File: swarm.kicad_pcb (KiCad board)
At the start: 2 copper layers, 1 part, among them U1 STM32F103RETx

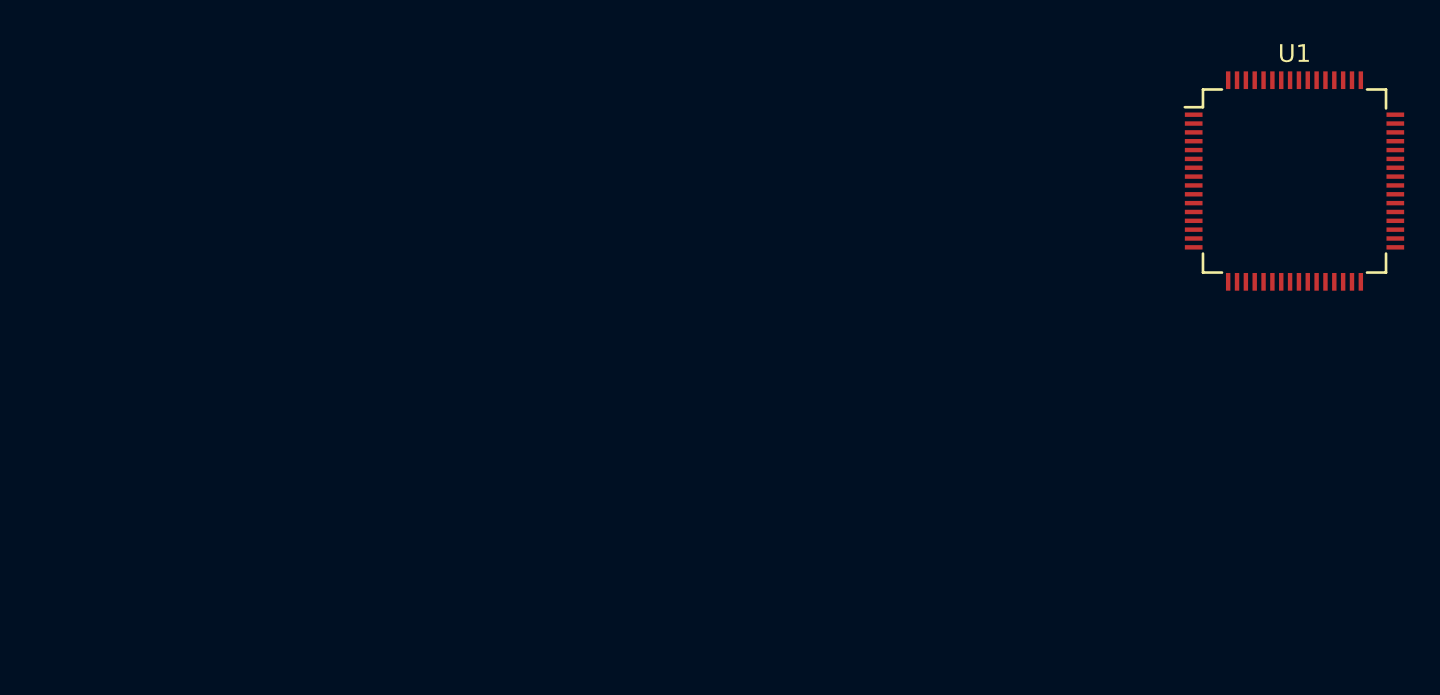
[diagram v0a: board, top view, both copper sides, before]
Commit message: Updates netlist, footprint selection
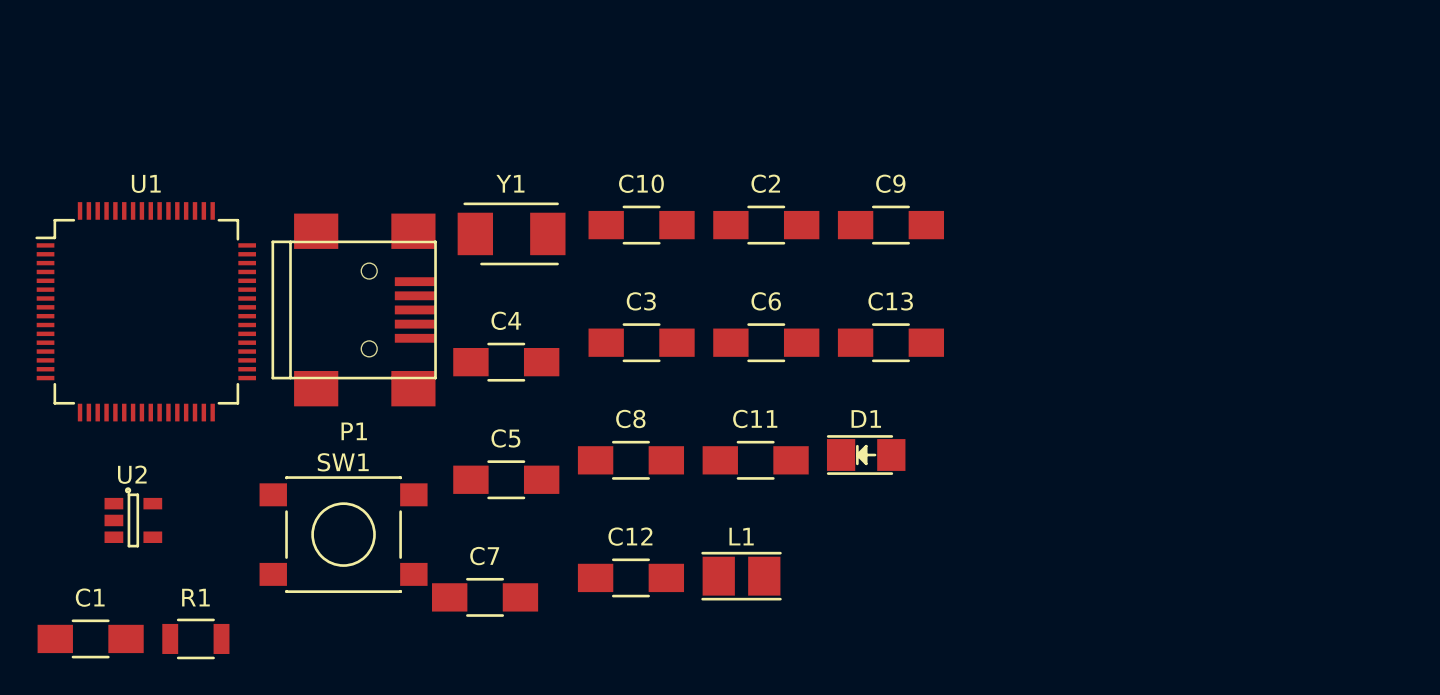
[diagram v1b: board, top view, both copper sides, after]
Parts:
- added C1: 10uF, Capacitors_SMD:C_1206_HandSoldering, F.Cu at (80.4, 130.9)
- added C10: 100n, Capacitors_SMD:C_1206_HandSoldering, F.Cu at (111.6, 107.5)
- added C11: 100n, Capacitors_SMD:C_1206_HandSoldering, F.Cu at (118.0, 120.8)
- added C12: 100n, Capacitors_SMD:C_1206_HandSoldering, F.Cu at (111.0, 127.4)
- added C13: 100n, Capacitors_SMD:C_1206_HandSoldering, F.Cu at (125.7, 114.1)
- added C2: 22uF, Capacitors_SMD:C_1206_HandSoldering, F.Cu at (118.6, 107.5)
- added C3: C, Capacitors_SMD:C_1206_HandSoldering, F.Cu at (111.6, 114.1)
- added C4: 100n, Capacitors_SMD:C_1206_HandSoldering, F.Cu at (103.9, 115.2)
- added C5: C, Capacitors_SMD:C_1206_HandSoldering, F.Cu at (103.9, 121.9)
- added C6: 1u, Capacitors_SMD:C_1206_HandSoldering, F.Cu at (118.6, 114.1)
- added C7: 10u, Capacitors_SMD:C_1206_HandSoldering, F.Cu at (102.7, 128.5)
- added C8: 100n, Capacitors_SMD:C_1206_HandSoldering, F.Cu at (111.0, 120.8)
- added C9: 100n, Capacitors_SMD:C_1206_HandSoldering, F.Cu at (125.7, 107.5)
- added D1: LED, LEDs:LED_1206, F.Cu at (124.3, 120.5)
- added L1: 2.2uH, Inductors:Inductor_Taiyo-Yuden_NR-24xx_HandSoldering, F.Cu at (117.2, 127.3)
- added P1: USB_OTG, Connect:USB_Mini-B, F.Cu at (95.3, 112.3)
- added R1: 330, Resistors_SMD:R_1206, F.Cu at (86.4, 130.9)
- added SW1: SW_PUSH, Buttons_Switches_SMD:SW_SPST_PTS645, F.Cu at (94.7, 125.0)
- added U2: LM3671MF-3.3, TO_SOT_Packages_SMD:SOT-23-5, F.Cu at (82.9, 124.2)
- added Y1: Crystal, Crystals:Crystal_SMD_5032_2Pads, F.Cu at (104.2, 108.0)
- moved U1 65.3 mm to (83.6, 112.4)
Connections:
- U1 pad 1: (no net) -> +3V3
- U1 pad 10: (no net) -> Net-(U1-Pad10)
- U1 pad 11: (no net) -> Net-(U1-Pad11)
- U1 pad 14: (no net) -> Net-(U1-Pad14)
- U1 pad 15: (no net) -> Net-(U1-Pad15)
- U1 pad 16: (no net) -> Net-(U1-Pad16)
- U1 pad 17: (no net) -> Net-(U1-Pad17)
- U1 pad 2: (no net) -> Net-(U1-Pad2)
- U1 pad 20: (no net) -> Net-(U1-Pad20)
- U1 pad 21: (no net) -> Net-(U1-Pad21)
- U1 pad 22: (no net) -> Net-(U1-Pad22)
- U1 pad 23: (no net) -> Net-(U1-Pad23)
- U1 pad 24: (no net) -> Net-(U1-Pad24)
- U1 pad 25: (no net) -> Net-(U1-Pad25)
- U1 pad 26: (no net) -> /LCD_PB0
- U1 pad 27: (no net) -> /LCD_PB1
- U1 pad 28: (no net) -> /LCD_PB2
- U1 pad 29: (no net) -> /LCD_PB10
- U1 pad 3: (no net) -> Net-(U1-Pad3)
- U1 pad 30: (no net) -> /LCD_PB11
- U1 pad 33: (no net) -> /LCD_PB12
- U1 pad 34: (no net) -> /LCD_PB13
- U1 pad 35: (no net) -> /LCD_PB14
- U1 pad 36: (no net) -> /LCD_PB15
- U1 pad 37: (no net) -> Net-(U1-Pad37)
- U1 pad 38: (no net) -> Net-(U1-Pad38)
- U1 pad 39: (no net) -> Net-(U1-Pad39)
- U1 pad 4: (no net) -> Net-(U1-Pad4)
- U1 pad 40: (no net) -> Net-(U1-Pad40)
- U1 pad 41: (no net) -> Net-(U1-Pad41)
- U1 pad 42: (no net) -> Net-(U1-Pad42)
- U1 pad 43: (no net) -> Net-(U1-Pad43)
- U1 pad 44: (no net) -> Net-(U1-Pad44)
- U1 pad 45: (no net) -> Net-(U1-Pad45)
- U1 pad 46: (no net) -> Net-(U1-Pad46)
- U1 pad 49: (no net) -> Net-(U1-Pad49)
- U1 pad 5: (no net) -> Net-(C3-Pad1)
- U1 pad 50: (no net) -> Net-(U1-Pad50)
- U1 pad 51: (no net) -> Net-(U1-Pad51)
- U1 pad 52: (no net) -> Net-(U1-Pad52)
- U1 pad 53: (no net) -> Net-(U1-Pad53)
- U1 pad 54: (no net) -> Net-(U1-Pad54)
- U1 pad 55: (no net) -> /LCD_PB3
- U1 pad 56: (no net) -> /LCD_PB4
- U1 pad 57: (no net) -> /LCD_PB5
- U1 pad 58: (no net) -> /LCD_PB6
- U1 pad 59: (no net) -> /LCD_PB7
- U1 pad 6: (no net) -> Net-(C5-Pad1)
- U1 pad 60: (no net) -> Net-(U1-Pad60)
- U1 pad 61: (no net) -> /LCD_PB8
- U1 pad 62: (no net) -> /LCD_PB9
- U1 pad 7: (no net) -> Net-(C4-Pad1)
- U1 pad 8: (no net) -> Net-(U1-Pad8)
- U1 pad 9: (no net) -> Net-(U1-Pad9)

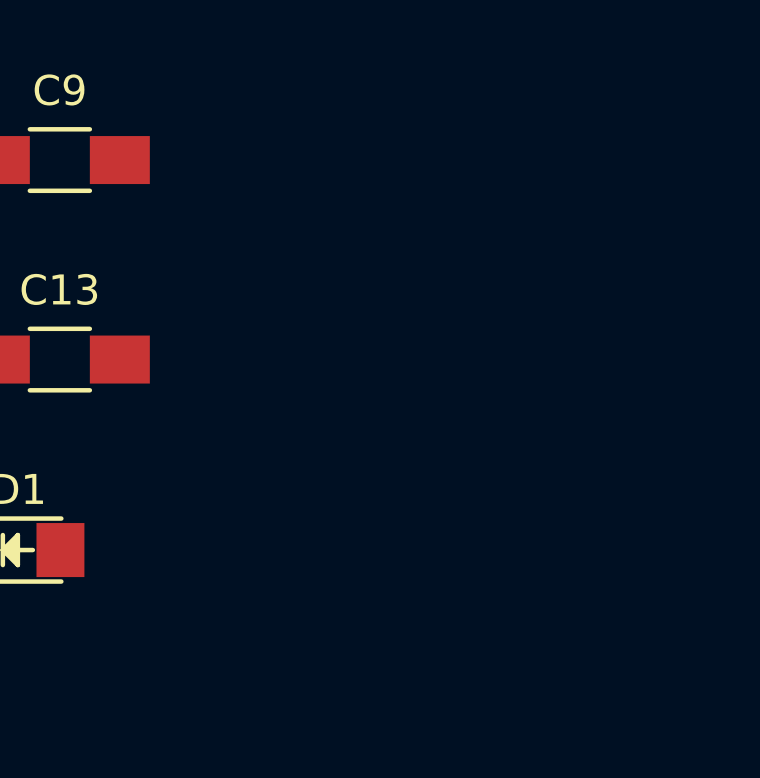
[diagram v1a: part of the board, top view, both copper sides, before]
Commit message: Adds MicroSD card and Mini USB connector via volium KiCad library
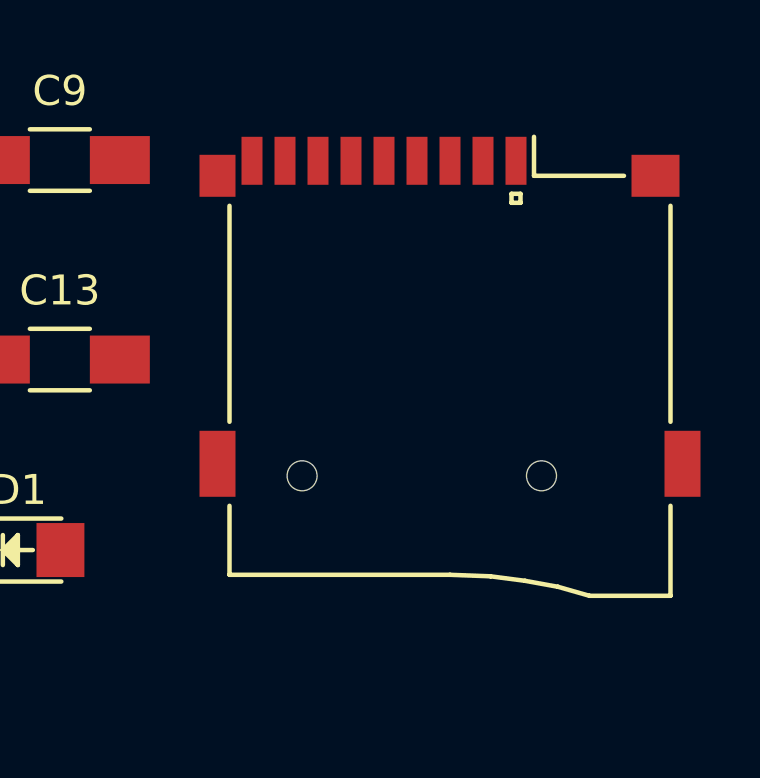
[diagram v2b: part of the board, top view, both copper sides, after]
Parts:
- added XS1: SD_ebay-uSD-push/push_SMD, volium:Conn_uSDcard, F.Cu at (138.7, 118.0)
- P1: footprint Connect:USB_Mini-B -> volium:USB_Mini-B

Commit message: Adds Micro SD card socket connection
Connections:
- net /LCD_PB0 renamed /LCD_D0
- net /LCD_PB1 renamed /LCD_D1
- net /LCD_PB10 renamed /LCD_D10
- net /LCD_PB11 renamed /LCD_D11
- net /LCD_PB12 renamed /LCD_D12
- net /LCD_PB13 renamed /LCD_D13
- net /LCD_PB14 renamed /LCD_D14
- net /LCD_PB15 renamed /LCD_D15
- net /LCD_PB2 renamed /LCD_D2
- net /LCD_PB3 renamed /LCD_D3
- net /LCD_PB4 renamed /LCD_D4
- net /LCD_PB5 renamed /LCD_D5
- net /LCD_PB6 renamed /LCD_D6
- net /LCD_PB7 renamed /LCD_D7
- net /LCD_PB8 renamed /LCD_D8
- net /LCD_PB9 renamed /LCD_D9
- net Net-(XS1-Pad9) renamed /SDIO_CD
- U1 pad 39: Net-(U1-Pad39) -> /SDIO_D0
- U1 pad 40: Net-(U1-Pad40) -> /SDIO_D1
- U1 pad 51: Net-(U1-Pad51) -> /SDIO_D2
- U1 pad 52: Net-(U1-Pad52) -> /SDIO_D3
- U1 pad 53: Net-(U1-Pad53) -> /SDIO_CLK
- U1 pad 54: Net-(U1-Pad54) -> /SDIO_CMD
- XS1 pad 1: Net-(XS1-Pad1) -> /SDIO_D2
- XS1 pad 2: Net-(XS1-Pad2) -> /SDIO_D3
- XS1 pad 3: Net-(XS1-Pad3) -> /SDIO_CMD
- XS1 pad 4: Net-(XS1-Pad4) -> GND
- XS1 pad 5: Net-(XS1-Pad5) -> /SDIO_CLK
- XS1 pad 6: Net-(XS1-Pad6) -> +3V3
- XS1 pad 7: Net-(XS1-Pad7) -> /SDIO_D0
- XS1 pad 8: Net-(XS1-Pad8) -> /SDIO_D1

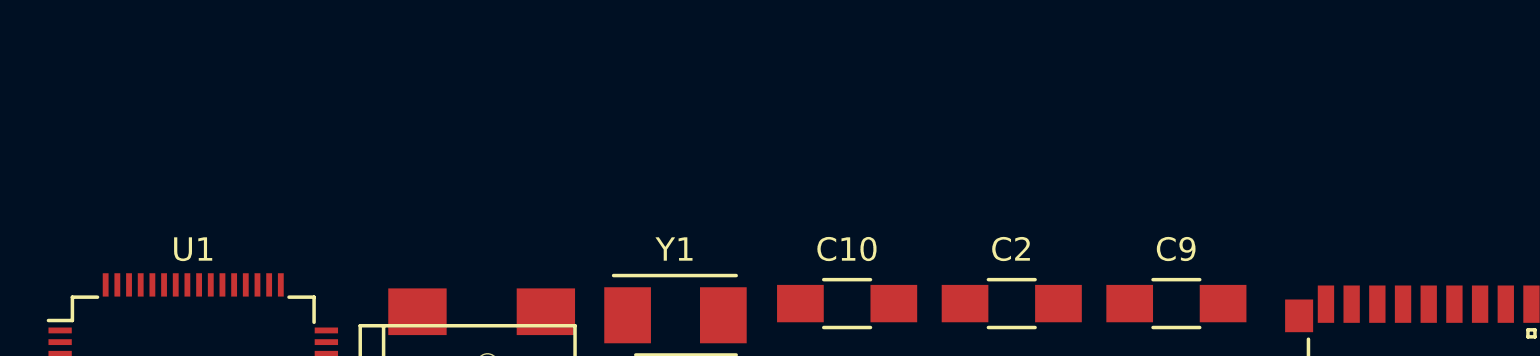
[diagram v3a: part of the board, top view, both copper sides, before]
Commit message: Adds LCD connector 2x20 pins
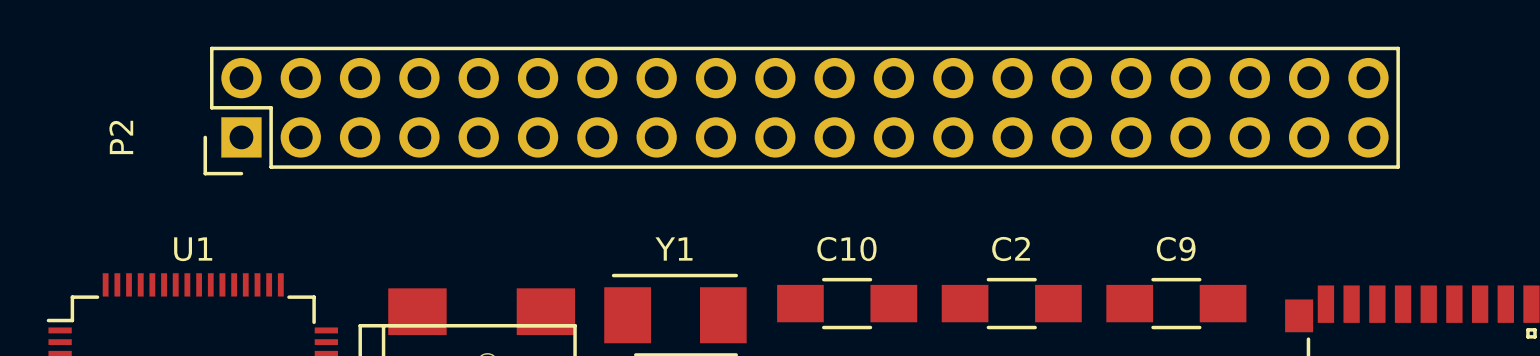
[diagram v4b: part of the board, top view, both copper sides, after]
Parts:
- added P2: CONN_02X20, Pin_Headers:Pin_Header_Straight_2x20, F.Cu at (85.7, 100.4)
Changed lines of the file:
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@@
 (kicad_pcb (version 4) (host pcbnew 4.0.4-stable)
   (general
-    (links 67)
-    (no_connects 67)
+    (links 84)
+    (no_connects 84)
     (area 0 0 0 0)
     (thickness 1.6)
@@
     (tracks 0)
     (zones 0)
-    (modules 22)
-    (nets 63)
+    (modules 23)
+    (nets 86)
   )
   (page A4)
@@
   (net 61 /LCD_D9)
   (net 62 /SDIO_CD)
+  (net 63 "Net-(P2-Pad5)")
+  (net 64 "Net-(P2-Pad18)")
+  (net 65 "Net-(P2-Pad20)")
+  (net 66 "Net-(P2-Pad22)")
+  (net 67 "Net-(P2-Pad24)")
+  (net 68 "Net-(P2-Pad26)")
+  (net 69 "Net-(P2-Pad28)")
+  (net 70 "Net-(P2-Pad30)")
+  (net 71 "Net-(P2-Pad31)")
+  (net 72 "Net-(P2-Pad32)")
+  (net 73 "Net-(P2-Pad34)")
+  (net 74 "Net-(P2-Pad35)")
+  (net 75 "Net-(P2-Pad36)")
+  (net 76 "Net-(P2-Pad37)")
+  (net 77 "Net-(P2-Pad38)")
+  (net 78 "Net-(P2-Pad39)")
+  (net 79 "Net-(P2-Pad40)")
+  (net 80 /LCD_RST)
+  (net 81 /LCD_CS)
+  (net 82 /LCD_RD)
+  (net 83 /LCD_WR)
+  (net 84 /LCD_RS)
+  (net 85 /+3.3V)
   (net_class Default "This is the default net class."
     (clearance 0.2)
@@
     (uvia_drill 0.1)
     (add_net +3V3)
+    (add_net /+3.3V)
+    (add_net /LCD_CS)
     (add_net /LCD_D0)
     (add_net /LCD_D1)
@@
     (add_net /LCD_D8)
     (add_net /LCD_D9)
+    (add_net /LCD_RD)
+    (add_net /LCD_RS)
+    (add_net /LCD_RST)
+    (add_net /LCD_WR)
     (add_net /SDIO_CD)
     (add_net /SDIO_CLK)
@@
     (add_net "Net-(P1-Pad3)")
     (add_net "Net-(P1-Pad4)")
+    (add_net "Net-(P2-Pad18)")
+    (add_net "Net-(P2-Pad20)")
+    (add_net "Net-(P2-Pad22)")
+    (add_net "Net-(P2-Pad24)")
+    (add_net "Net-(P2-Pad26)")
+    (add_net "Net-(P2-Pad28)")
+    (add_net "Net-(P2-Pad30)")
+    (add_net "Net-(P2-Pad31)")
+    (add_net "Net-(P2-Pad32)")
+    (add_net "Net-(P2-Pad34)")
+    (add_net "Net-(P2-Pad35)")
+    (add_net "Net-(P2-Pad36)")
+    (add_net "Net-(P2-Pad37)")
+    (add_net "Net-(P2-Pad38)")
+    (add_net "Net-(P2-Pad39)")
+    (add_net "Net-(P2-Pad40)")
+    (add_net "Net-(P2-Pad5)")
     (add_net "Net-(U1-Pad10)")
     (add_net "Net-(U1-Pad11)")
@@
     )
   )
+  (module Pin_Headers:Pin_Header_Straight_2x20 (layer F.Cu)
+    (at 85.65 100.38 90)
+    (descr "Through hole pin header")
+    (tags "pin header")
+    (fp_text reference P2 (at 0 -5.1 90) (layer F.SilkS)
+      (effects (font (size 1 1) (thickness 0.15)))
+    )
+    (fp_text value CONN_02X20 (at 0 -3.1 90) (layer F.Fab)
+      (effects (font (size 1 1) (thickness 0.15)))
+    )
+    (fp_line (start -1.75 -1.75) (end -1.75 50.05) (layer F.CrtYd) (width 0.05))
+    (fp_line (start 4.3 -1.75) (end 4.3 50.05) (layer F.CrtYd) (width 0.05))
+    (fp_line (start -1.75 -1.75) (end 4.3 -1.75) (layer F.CrtYd) (width 0.05))
+    (fp_line (start -1.75 50.05) (end 4.3 50.05) (layer F.CrtYd) (width 0.05))
+    (fp_line (start 3.81 49.53) (end 3.81 -1.27) (layer F.SilkS) (width 0.15))
+    (fp_line (start -1.27 1.27) (end -1.27 49.53) (layer F.SilkS) (width 0.15))
+    (fp_line (start 3.81 49.53) (end -1.27 49.53) (layer F.SilkS) (width 0.15))
+    (fp_line (start 3.81 -1.27) (end 1.27 -1.27) (layer F.SilkS) (width 0.15))
+    (fp_line (start 0 -1.55) (end -1.55 -1.55) (layer F.SilkS) (width 0.15))
+    (fp_line (start 1.27 -1.27) (end 1.27 1.27) (layer F.SilkS) (width 0.15))
+    (fp_line (start 1.27 1.27) (end -1.27 1.27) (layer F.SilkS) (width 0.15))
+    (fp_line (start -1.55 -1.55) (end -1.55 0) (layer F.SilkS) (width 0.15))
+    (pad 1 thru_hole rect (at 0 0 90) (size 1.7272 1.7272) (drill 1.016) (layers *.Cu *.Mask)
+      (net 1 GND))
+    (pad 2 thru_hole oval (at 2.54 0 90) (size 1.7272 1.7272) (drill 1.016) (layers *.Cu *.Mask)
+      (net 40 /LCD_D0))
+    (pad 3 thru_hole oval (at 0 2.54 90) (size 1.7272 1.7272) (drill 1.016) (layers *.Cu *.Mask)
+      (net 85 /+3.3V))
+    (pad 4 thru_hole oval (at 2.54 2.54 90) (size 1.7272 1.7272) (drill 1.016) (layers *.Cu *.Mask)
+      (net 41 /LCD_D1))
+    (pad 5 thru_hole oval (at 0 5.08 90) (size 1.7272 1.7272) (drill 1.016) (layers *.Cu *.Mask)
+      (net 63 "Net-(P2-Pad5)"))
+    (pad 6 thru_hole oval (at 2.54 5.08 90) (size 1.7272 1.7272) (drill 1.016) (layers *.Cu *.Mask)
+      (net 42 /LCD_D2))
+    (pad 7 thru_hole oval (at 0 7.62 90) (size 1.7272 1.7272) (drill 1.016) (layers *.Cu *.Mask)
+      (net 84 /LCD_RS))
+    (pad 8 thru_hole oval (at 2.54 7.62 90) (size 1.7272 1.7272) (drill 1.016) (layers *.Cu *.Mask)
+      (net 55 /LCD_D3))
+    (pad 9 thru_hole oval (at 0 10.16 90) (size 1.7272 1.7272) (drill 1.016) (layers *.Cu *.Mask)
+      (net 83 /LCD_WR))
+    (pad 10 thru_hole oval (at 2.54 10.16 90) (size 1.7272 1.7272) (drill 1.016) (layers *.Cu *.Mask)
+      (net 56 /LCD_D4))
+    (pad 11 thru_hole oval (at 0 12.7 90) (size 1.7272 1.7272) (drill 1.016) (layers *.Cu *.Mask)
+      (net 82 /LCD_RD))
+    (pad 12 thru_hole oval (at 2.54 12.7 90) (size 1.7272 1.7272) (drill 1.016) (layers *.Cu *.Mask)
+      (net 57 /LCD_D5))
+    (pad 13 thru_hole oval (at 0 15.24 90) (size 1.7272 1.7272) (drill 1.016) (layers *.Cu *.Mask)
+      (net 60 /LCD_D8))
+    (pad 14 thru_hole oval (at 2.54 15.24 90) (size 1.7272 1.7272) (drill 1.016) (layers *.Cu *.Mask)
+      (net 58 /LCD_D6))
+    (pad 15 thru_hole oval (at 0 17.78 90) (size 1.7272 1.7272) (drill 1.016) (layers *.Cu *.Mask)
+      (net 61 /LCD_D9))
+    (pad 16 thru_hole oval (at 2.54 17.78 90) (size 1.7272 1.7272) (drill 1.016) (layers *.Cu *.Mask)
+      (net 59 /LCD_D7))
+    (pad 17 thru_hole oval (at 0 20.32 90) (size 1.7272 1.7272) (drill 1.016) (layers *.Cu *.Mask)
+      (net 43 /LCD_D10))
+    (pad 18 thru_hole oval (at 2.54 20.32 90) (size 1.7272 1.7272) (drill 1.016) (layers *.Cu *.Mask)
+      (net 64 "Net-(P2-Pad18)"))
+    (pad 19 thru_hole oval (at 0 22.86 90) (size 1.7272 1.7272) (drill 1.016) (layers *.Cu *.Mask)
+      (net 44 /LCD_D11))
+    (pad 20 thru_hole oval (at 2.54 22.86 90) (size 1.7272 1.7272) (drill 1.016) (layers *.Cu *.Mask)
+      (net 65 "Net-(P2-Pad20)"))
+    (pad 21 thru_hole oval (at 0 25.4 90) (size 1.7272 1.7272) (drill 1.016) (layers *.Cu *.Mask)
+      (net 45 /LCD_D12))
+    (pad 22 thru_hole oval (at 2.54 25.4 90) (size 1.7272 1.7272) (drill 1.016) (layers *.Cu *.Mask)
+      (net 66 "Net-(P2-Pad22)"))
+    (pad 23 thru_hole oval (at 0 27.94 90) (size 1.7272 1.7272) (drill 1.016) (layers *.Cu *.Mask)
+      (net 46 /LCD_D13))
+    (pad 24 thru_hole oval (at 2.54 27.94 90) (size 1.7272 1.7272) (drill 1.016) (layers *.Cu *.Mask)
+      (net 67 "Net-(P2-Pad24)"))
+    (pad 25 thru_hole oval (at 0 30.48 90) (size 1.7272 1.7272) (drill 1.016) (layers *.Cu *.Mask)
+      (net 47 /LCD_D14))
+    (pad 26 thru_hole oval (at 2.54 30.48 90) (size 1.7272 1.7272) (drill 1.016) (layers *.Cu *.Mask)
+      (net 68 "Net-(P2-Pad26)"))
+    (pad 27 thru_hole oval (at 0 33.02 90) (size 1.7272 1.7272) (drill 1.016) (layers *.Cu *.Mask)
+      (net 48 /LCD_D15))
+    (pad 28 thru_hole oval (at 2.54 33.02 90) (size 1.7272 1.7272) (drill 1.016) (layers *.Cu *.Mask)
+      (net 69 "Net-(P2-Pad28)"))
+    (pad 29 thru_hole oval (at 0 35.56 90) (size 1.7272 1.7272) (drill 1.016) (layers *.Cu *.Mask)
+      (net 81 /LCD_CS))
+    (pad 30 thru_hole oval (at 2.54 35.56 90) (size 1.7272 1.7272) (drill 1.016) (layers *.Cu *.Mask)
+      (net 70 "Net-(P2-Pad30)"))
+    (pad 31 thru_hole oval (at 0 38.1 90) (size 1.7272 1.7272) (drill 1.016) (layers *.Cu *.Mask)
+      (net 71 "Net-(P2-Pad31)"))
+    (pad 32 thru_hole oval (at 2.54 38.1 90) (size 1.7272 1.7272) (drill 1.016) (layers *.Cu *.Mask)
+      (net 72 "Net-(P2-Pad32)"))
+    (pad 33 thru_hole oval (at 0 40.64 90) (size 1.7272 1.7272) (drill 1.016) (layers *.Cu *.Mask)
+      (net 80 /LCD_RST))
+    (pad 34 thru_hole oval (at 2.54 40.64 90) (size 1.7272 1.7272) (drill 1.016) (layers *.Cu *.Mask)
+      (net 73 "Net-(P2-Pad34)"))
+    (pad 35 thru_hole oval (at 0 43.18 90) (size 1.7272 1.7272) (drill 1.016) (layers *.Cu *.Mask)
+      (net 74 "Net-(P2-Pad35)"))
+    (pad 36 thru_hole oval (at 2.54 43.18 90) (size 1.7272 1.7272) (drill 1.016) (layers *.Cu *.Mask)
+      (net 75 "Net-(P2-Pad36)"))
+    (pad 37 thru_hole oval (at 0 45.72 90) (size 1.7272 1.7272) (drill 1.016) (layers *.Cu *.Mask)
+      (net 76 "Net-(P2-Pad37)"))
+    (pad 38 thru_hole oval (at 2.54 45.72 90) (size 1.7272 1.7272) (drill 1.016) (layers *.Cu *.Mask)
+      (net 77 "Net-(P2-Pad38)"))
+    (pad 39 thru_hole oval (at 0 48.26 90) (size 1.7272 1.7272) (drill 1.016) (layers *.Cu *.Mask)
+      (net 78 "Net-(P2-Pad39)"))
+    (pad 40 thru_hole oval (at 2.54 48.26 90) (size 1.7272 1.7272) (drill 1.016) (layers *.Cu *.Mask)
+      (net 79 "Net-(P2-Pad40)"))
+    (model Pin_Headers.3dshapes/Pin_Header_Straight_2x20.wrl
+      (at (xyz 0.05 -0.95 0))
+      (scale (xyz 1 1 1))
+      (rotate (xyz 0 0 90))
+    )
+  )
